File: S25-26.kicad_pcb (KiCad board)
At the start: 6 copper layers, 90 x 90 mm, 120 parts, among them IC1 CMV4000-3E5M0PN, IC10 DS90LV048ATM_NOPB, IC2 MXL86110I-AQB-R, IC3 NCV317BD2TR4G, IC4 MT29F2G01ABAGDWB-IT_G_TR, IC5 MT29F2G01ABAGDWB-IT_G_TR, IC6 XMC7200D-E272K8384AA, IC7 DS90LV011AHMF_NOPB, IC8 DS90LV048ATM_NOPB, IC9 DS90LV048ATM_NOPB, J1 DC_IN_PADS, J3 Conn_01x02_Pin, J4 RJ45_RB1-125B8G1A, Q1 ZXT849K, U1 TPS73601MDRBREP, U2 TPS73601MDRBREP, Y1 DSC1101DM2-012.0000

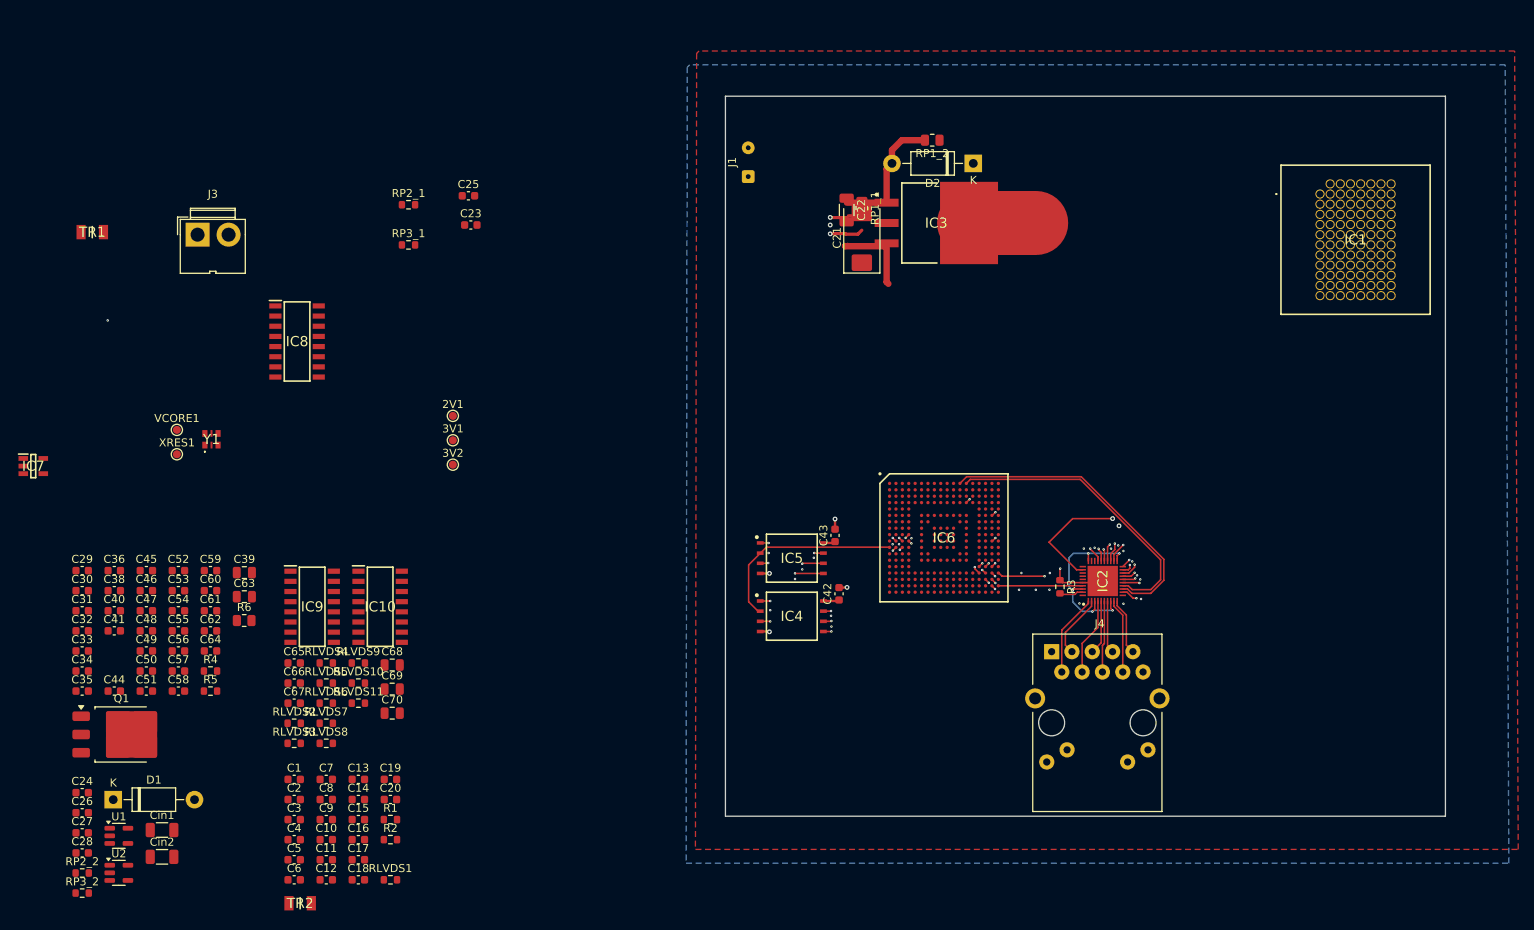
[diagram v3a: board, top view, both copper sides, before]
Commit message: Lots of PCB changes, some small parts changes
Updated parts footprints from those found in MDE Lab. Some parameters may be incorrect, but all footprints should be correct
Drew most of PCB. CMOS SPI still needs connection. Decoupling caps on MCU still need connection. Power and ground needs to be analyzed, and some components may not have power or ground connected.
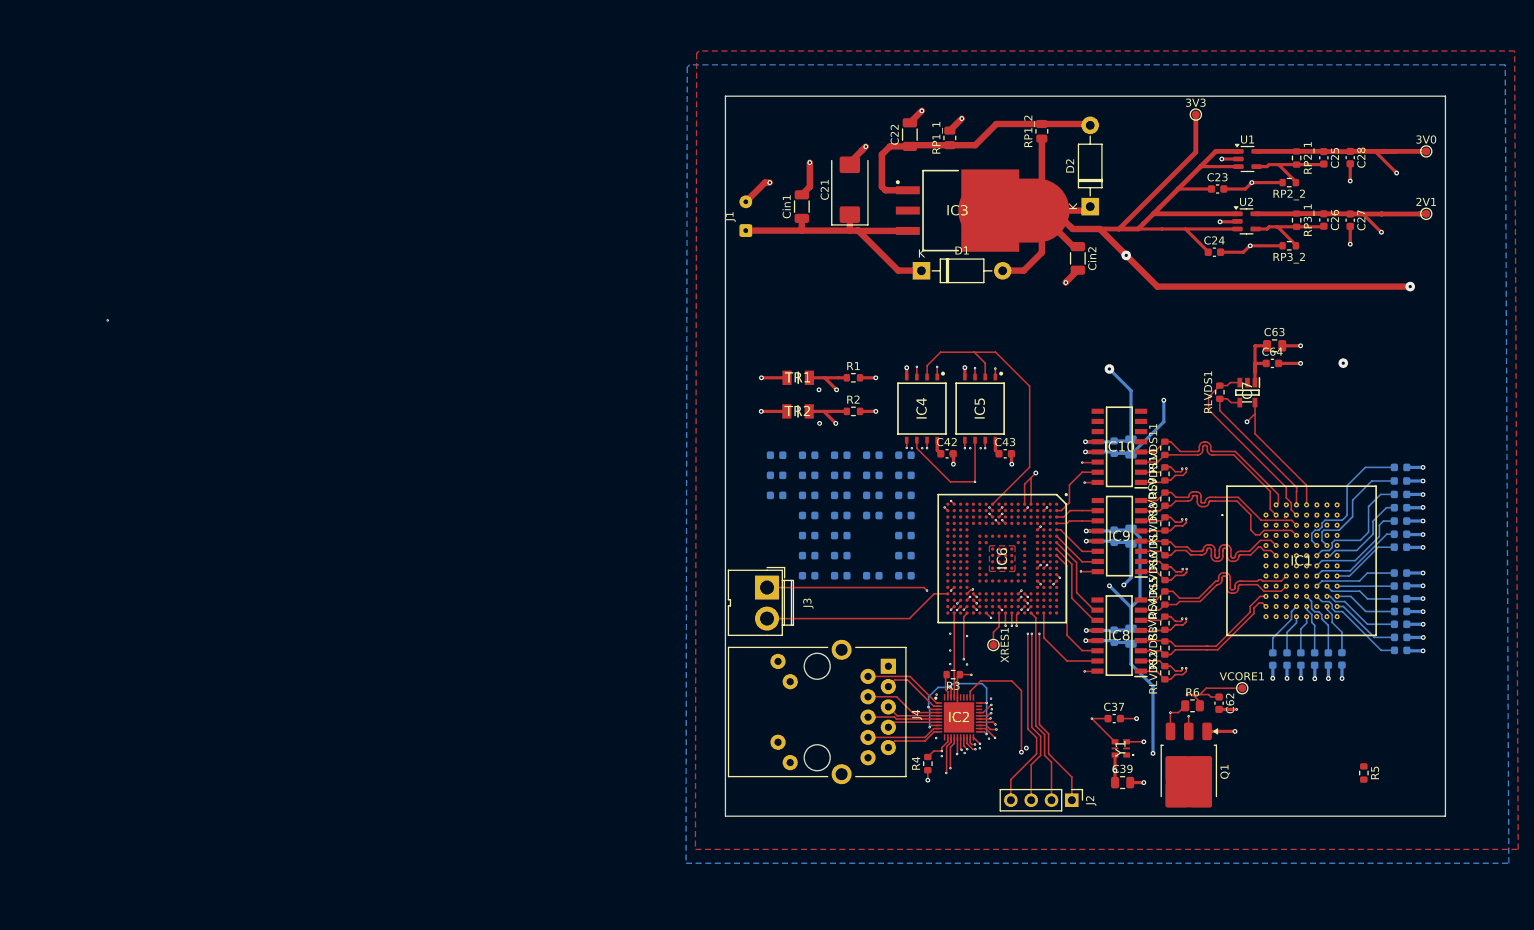
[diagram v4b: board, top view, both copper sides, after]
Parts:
- removed 3V1, 3V2: TestPoint, TestPoint:TestPoint_Pad_D1.0mm
- added 3V0: TestPoint, TestPoint:TestPoint_Pad_D1.0mm, F.Cu at (196.0, 57.1)
- added 3V3: TestPoint, TestPoint:TestPoint_Pad_D1.0mm, F.Cu at (167.2, 52.5)
- added C37: 15pF, Capacitor_SMD:C_0603_1608Metric, F.Cu at (157.0, 128.0)
- added J2: Conn_01x04_Pin, Connector_PinHeader_2.54mm:PinHeader_1x04_P2.54mm_Vertical, F.Cu at (151.7, 138.2)
- C1, C10, C11, C12, C13, C14, C15, C16, C17, C18, C19, C2, C20, C29, C3, C30, C31, C32, C33, C34, C35, C36, C38, C4, C40, C41, C44, C45, C46, C47, C48, C49, C5, C50, C51, C52, C53, C54, C55, C56, C57, C58, C59, C6, C60, C61, C65, C66, C67, C68, C69, C7, C70, C8, C9: moved to B.Cu
- moved C28 180.8 mm to (186.5, 57.9), turned to -90 degrees
- moved C27 176.0 mm to (186.5, 65.7), turned to -90 degrees
- moved RP2_2 173.8 mm to (178.9, 61.0), turned to 180 degrees
- moved C26 172.0 mm to (183.2, 65.7), turned to -90 degrees
- moved RP3_2 171.2 mm to (178.9, 68.9), turned to 180 degrees
- moved U1 164.5 mm to (173.7, 58.0)
- moved U2 162.8 mm to (173.5, 65.8)
- moved C24 156.8 mm to (169.5, 69.7)
- moved IC7 152.0 mm to (173.7, 87.2), turned to -90 degrees
- moved C5 146.7 mm to (192.8, 96.6), turned to 180 degrees
- moved C6 146.4 mm to (192.8, 100.0), turned to 180 degrees
- moved R5 144.5 mm to (188.2, 134.8), turned to -90 degrees
- moved C10 141.6 mm to (192.8, 98.3), turned to 180 degrees
- moved C11 141.3 mm to (192.8, 101.6), turned to 180 degrees
- moved C1 139.2 mm to (192.8, 119.5), turned to 180 degrees
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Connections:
- C47 pad 1: +3V3 -> /Processing/EXT_PS_CTL1
- C49 pad 1: +3V3 -> /Processing/EXT_PS_CTL1
- C51 pad 1: +3V3 -> /Processing/EXT_PS_CTL1
- C53 pad 1: +3V3 -> /Processing/EXT_PS_CTL1
- C54 pad 1: +3V3 -> /Processing/EXT_PS_CTL1
- C62 pad 1: +3V3 -> /Processing/EXT_PS_CTL1
- IC10 pad 1: /LVDS Conversion/LVDS_CLK_OUT_N -> /LVDS Conversion/LVDS_CH01_N
- IC10 pad 10: /LVDS Conversion/CMOS_CLK_OUT -> unconnected-(IC10-ROUT4-Pad10)
- IC10 pad 14: unconnected-(IC10-ROUT2-Pad14) -> /LVDS Conversion/CMOS_CTR_OUT
- IC10 pad 15: /LVDS Conversion/CMOS_CTR_OUT -> /LVDS Conversion/CMOS_CH01
- IC10 pad 2: /LVDS Conversion/LVDS_CLK_OUT_P -> /LVDS Conversion/LVDS_CH01_P
- IC10 pad 3: unconnected-(IC10-RIN2+-Pad3) -> /LVDS Conversion/LVDS_CTR_OUT_P
- IC10 pad 4: unconnected-(IC10-RIN2--Pad4) -> /LVDS Conversion/LVDS_CTR_OUT_N
- IC10 pad 7: /LVDS Conversion/LVDS_CTR_OUT_P -> unconnected-(IC10-RIN4+-Pad7)
- IC10 pad 8: /LVDS Conversion/LVDS_CTR_OUT_N -> unconnected-(IC10-RIN4--Pad8)
- IC6 pad A2: unconnected-(IC6B-P6.5-PadA2) -> /LVDS Conversion/CMOS_CH01
- IC6 pad A3: unconnected-(IC6B-P6.2-PadA3) -> /LVDS Conversion/CMOS_CH03
- IC6 pad A4: unconnected-(IC6B-P31.2-PadA4) -> /LVDS Conversion/CMOS_CH05
- IC6 pad A5: unconnected-(IC6B-P31.0-PadA5) -> /LVDS Conversion/CMOS_CH07
- IC6 pad A6: /LVDS Conversion/CMOS_CH01 -> /LVDS Conversion/CMOS_CH09
- IC6 pad A7: unconnected-(IC6B-P4.4-PadA7) -> /LVDS Conversion/CMOS_CH11
- IC6 pad A8: /LVDS Conversion/CMOS_CH03 -> /LVDS Conversion/CMOS_CH13
- IC6 pad A9: unconnected-(IC6B-P29.5-PadA9) -> /LVDS Conversion/CMOS_CH15
- IC6 pad B4: /Processing/TEMPR_ADC0 (P6.0) -> unconnected-(IC6B-P6.0-PadB4)
- IC6 pad B6: /LVDS Conversion/CMOS_CH11 -> unconnected-(IC6B-P5.1-PadB6)
- IC6 pad B8: /LVDS Conversion/CMOS_CH09 -> unconnected-(IC6B-P4.1-PadB8)
- IC6 pad C18: unconnected-(IC6B-P28.5-PadC18) -> /LVDS Conversion/CMOS_CLK_OUT
- IC6 pad C2: unconnected-(IC6B-P32.1-PadC2) -> /LVDS Conversion/CMOS_CTR_OUT
- IC6 pad C4: /Processing/TEMPR_ADC1 (P6.1) -> unconnected-(IC6B-P6.1-PadC4)
- IC6 pad C6: /LVDS Conversion/CMOS_CH05 -> unconnected-(IC6B-P5.2-PadC6)
- IC6 pad C8: /LVDS Conversion/CMOS_CH07 -> unconnected-(IC6B-P4.2-PadC8)
- IC6 pad D17: /LVDS Conversion/CMOS_CTR_OUT -> unconnected-(IC6B-P28.3-PadD17)
- IC6 pad D6: /LVDS Conversion/CMOS_CH15 -> unconnected-(IC6B-P5.3-PadD6)
- IC6 pad D8: /LVDS Conversion/CMOS_CH13 -> unconnected-(IC6B-P4.3-PadD8)
- IC6 pad F13: +3V3 -> /Processing/EXT_PS_CTL1
- IC6 pad F6: +3V3 -> /Processing/EXT_PS_CTL1
- IC6 pad G18: +3V3 -> /Processing/EXT_PS_CTL1
- IC6 pad J3: /LVDS Conversion/CMOS_CLK_OUT -> unconnected-(IC6B-P24.0-PadJ3)
- IC6 pad N13: +3V3 -> /Processing/EXT_PS_CTL1
- IC6 pad N6: +3V3 -> /Processing/EXT_PS_CTL1
- IC6 pad U1: unconnected-(IC6B-P12.6-PadU1) -> /Processing/TEMPR_ADC0 (P6.0)
- IC6 pad V2: unconnected-(IC6B-P13.0-PadV2) -> /Processing/TEMPR_ADC1 (P6.1)
- IC8 pad 1: /LVDS Conversion/LVDS_CH05_N -> /LVDS Conversion/LVDS_CLK_OUT_N
- IC8 pad 10: /LVDS Conversion/CMOS_CH13 -> /LVDS Conversion/CMOS_CH11
- IC8 pad 11: /LVDS Conversion/CMOS_CH07 -> /LVDS Conversion/CMOS_CH13
- IC8 pad 15: /LVDS Conversion/CMOS_CH05 -> /LVDS Conversion/CMOS_CLK_OUT
- IC8 pad 2: /LVDS Conversion/LVDS_CH05_P -> /LVDS Conversion/LVDS_CLK_OUT_P
- IC8 pad 5: /LVDS Conversion/LVDS_CH07_N -> /LVDS Conversion/LVDS_CH13_N
- IC8 pad 6: /LVDS Conversion/LVDS_CH07_P -> /LVDS Conversion/LVDS_CH13_P
- IC8 pad 7: /LVDS Conversion/LVDS_CH13_P -> /LVDS Conversion/LVDS_CH11_P
- IC8 pad 8: /LVDS Conversion/LVDS_CH13_N -> /LVDS Conversion/LVDS_CH11_N
- IC9 pad 1: /LVDS Conversion/LVDS_CH01_N -> /LVDS Conversion/LVDS_CH09_N
- IC9 pad 10: /LVDS Conversion/CMOS_CH09 -> /LVDS Conversion/CMOS_CH03
- IC9 pad 11: /LVDS Conversion/CMOS_CH03 -> /LVDS Conversion/CMOS_CH05
- IC9 pad 14: /LVDS Conversion/CMOS_CH11 -> /LVDS Conversion/CMOS_CH07
- IC9 pad 15: /LVDS Conversion/CMOS_CH01 -> /LVDS Conversion/CMOS_CH09
- IC9 pad 2: /LVDS Conversion/LVDS_CH01_P -> /LVDS Conversion/LVDS_CH09_P
- IC9 pad 3: /LVDS Conversion/LVDS_CH11_P -> /LVDS Conversion/LVDS_CH07_P
- IC9 pad 4: /LVDS Conversion/LVDS_CH11_N -> /LVDS Conversion/LVDS_CH07_N
- IC9 pad 5: /LVDS Conversion/LVDS_CH03_N -> /LVDS Conversion/LVDS_CH05_N
- IC9 pad 6: /LVDS Conversion/LVDS_CH03_P -> /LVDS Conversion/LVDS_CH05_P
- IC9 pad 7: /LVDS Conversion/LVDS_CH09_P -> /LVDS Conversion/LVDS_CH03_P
- IC9 pad 8: /LVDS Conversion/LVDS_CH09_N -> /LVDS Conversion/LVDS_CH03_N
- R6 pad 2: +3V3 -> /Processing/EXT_PS_CTL1
- RLVDS10 pad 1: /LVDS Conversion/LVDS_CLK_OUT_N -> /LVDS Conversion/LVDS_CH01_N
- RLVDS10 pad 2: /LVDS Conversion/LVDS_CLK_OUT_P -> /LVDS Conversion/LVDS_CH01_P
- RLVDS2 pad 1: /LVDS Conversion/LVDS_CH05_N -> /LVDS Conversion/LVDS_CLK_OUT_N
- RLVDS2 pad 2: /LVDS Conversion/LVDS_CH05_P -> /LVDS Conversion/LVDS_CLK_OUT_P
- RLVDS4 pad 1: /LVDS Conversion/LVDS_CH07_N -> /LVDS Conversion/LVDS_CH13_N
- RLVDS4 pad 2: /LVDS Conversion/LVDS_CH07_P -> /LVDS Conversion/LVDS_CH13_P
- RLVDS5 pad 1: /LVDS Conversion/LVDS_CH13_P -> /LVDS Conversion/LVDS_CH11_P
- RLVDS5 pad 2: /LVDS Conversion/LVDS_CH13_N -> /LVDS Conversion/LVDS_CH11_N
- RLVDS6 pad 1: /LVDS Conversion/LVDS_CH01_N -> /LVDS Conversion/LVDS_CH09_N
- RLVDS6 pad 2: /LVDS Conversion/LVDS_CH01_P -> /LVDS Conversion/LVDS_CH09_P
- RLVDS7 pad 1: /LVDS Conversion/LVDS_CH11_P -> /LVDS Conversion/LVDS_CH07_P
- RLVDS7 pad 2: /LVDS Conversion/LVDS_CH11_N -> /LVDS Conversion/LVDS_CH07_N
- RLVDS8 pad 1: /LVDS Conversion/LVDS_CH03_N -> /LVDS Conversion/LVDS_CH05_N
- RLVDS8 pad 2: /LVDS Conversion/LVDS_CH03_P -> /LVDS Conversion/LVDS_CH05_P
- RLVDS9 pad 1: /LVDS Conversion/LVDS_CH09_P -> /LVDS Conversion/LVDS_CH03_P
- RLVDS9 pad 2: /LVDS Conversion/LVDS_CH09_N -> /LVDS Conversion/LVDS_CH03_N
- VCORE1 pad 1: +3V3 -> /Processing/EXT_PS_CTL1
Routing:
- net GND: track 19.9 -> 462.0 mm, vias 35 -> 67
- net +3V3: track 11.9 -> 451.2 mm, vias 0 -> 17
- net +3V: track 0.00 -> 94.7 mm, vias 0 -> 1
- net +2V1: track 0.00 -> 80.8 mm, vias 0 -> 1
- net /CMOS_MASTER_CLK: track 0.00 -> 53.7 mm, vias 0 -> 2
- net /Processing/EXT_PS_CTL1: track 0.00 -> 38.2 mm, vias 0 -> 2
- net /LVDS Conversion/LVDS_RECV_EN: track 0.00 -> 36.5 mm, vias 0 -> 4
- net Net-(D2-A): track 0.00 -> 35.1 mm
- net /Processing/DRV_VOUT: track 0.00 -> 31.2 mm, vias 0 -> 2
- net /Processing/EXT_PS_CTL0: track 0.00 -> 30.8 mm, vias 0 -> 2
- net /Processing/TEMPR_ADC0 (P6.0): track 0.00 -> 30.0 mm, vias 0 -> 2
- net /JTAG_SWCLK: track 0.00 -> 28.2 mm, vias 0 -> 2
- net /Processing/TEMPR_ADC1 (P6.1): track 0.00 -> 26.7 mm, vias 0 -> 2
- net /JTAG_SWO: track 0.00 -> 26.3 mm, vias 0 -> 2
- net /JTAG_TDI: track 0.00 -> 26.2 mm, vias 0 -> 2
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- added copper zone on F.Cu, net GND

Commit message: Adjusted board setup for AdvancedPCB; fixed many DRC errors
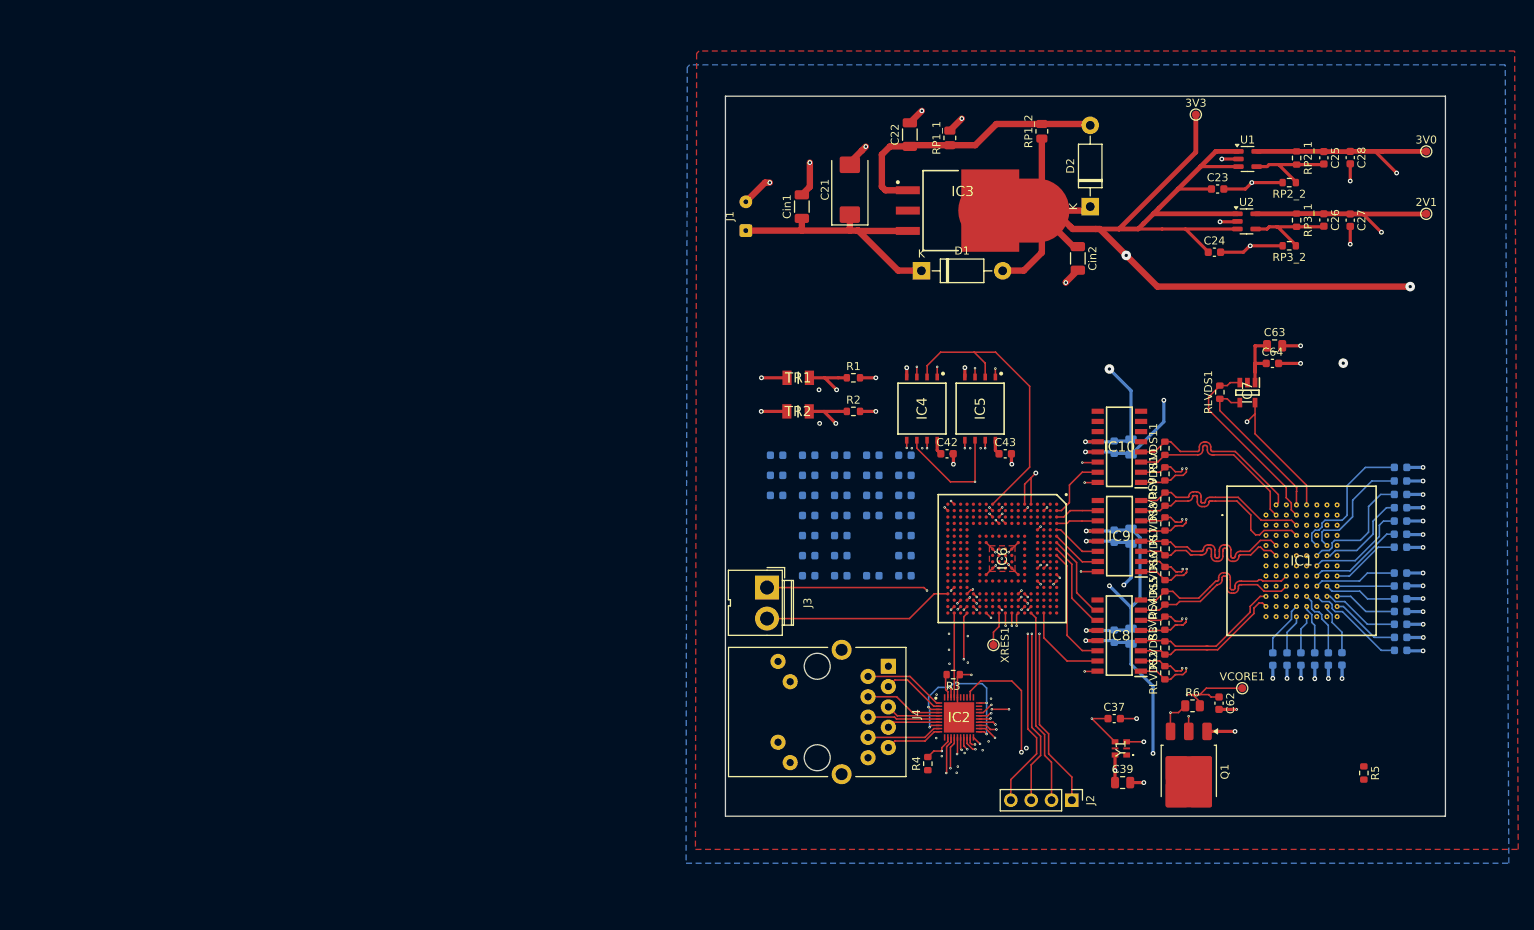
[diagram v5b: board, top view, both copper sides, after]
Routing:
- net GND: track 462.0 -> 473.6 mm, vias 67 -> 75
- net /ETH0_TXD_2: track 27.1 -> 28.9 mm
- net +3V: track 94.7 -> 93.1 mm
- net +3V3: track 451.2 -> 450.0 mm, vias 17 -> 16
- net /ETH0_TXD_0: track 21.3 -> 22.3 mm
- net (no net): vias 1 -> 0

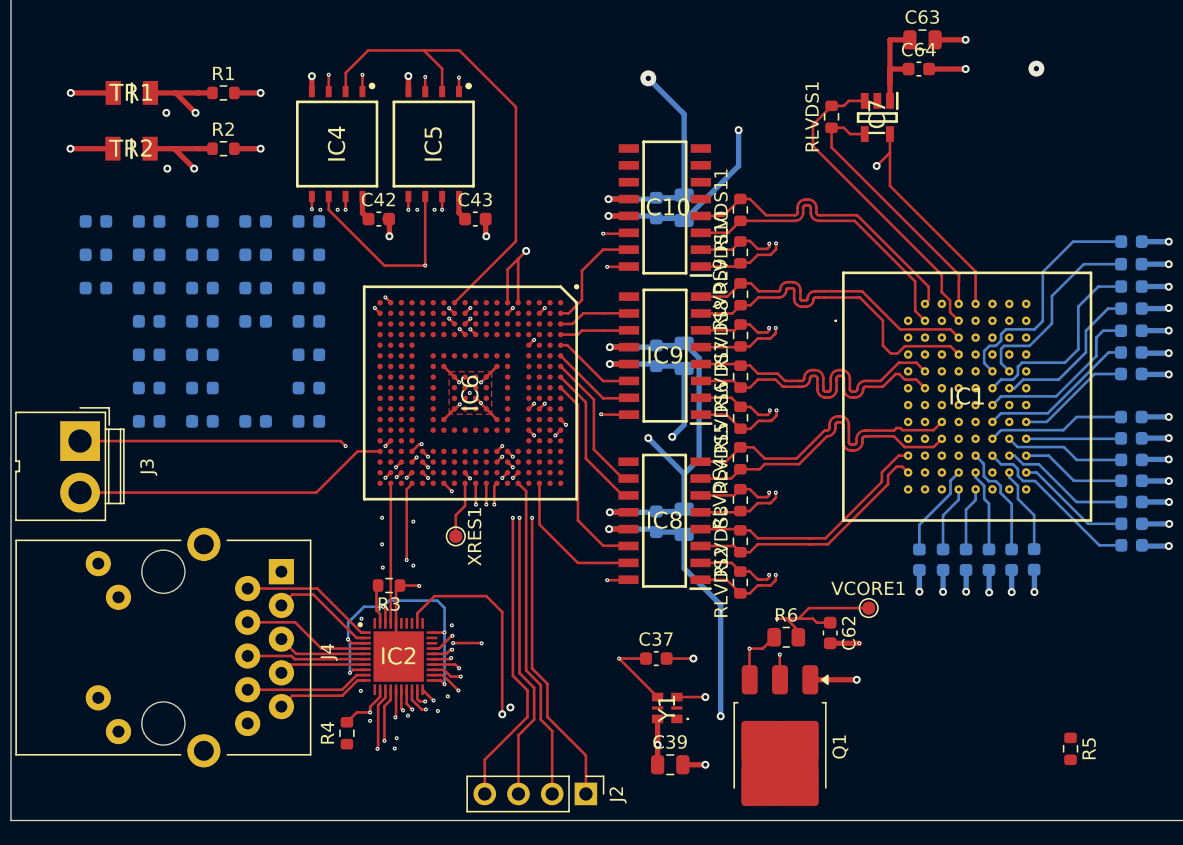
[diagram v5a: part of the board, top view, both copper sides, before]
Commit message: Fixed DRC; all connections made
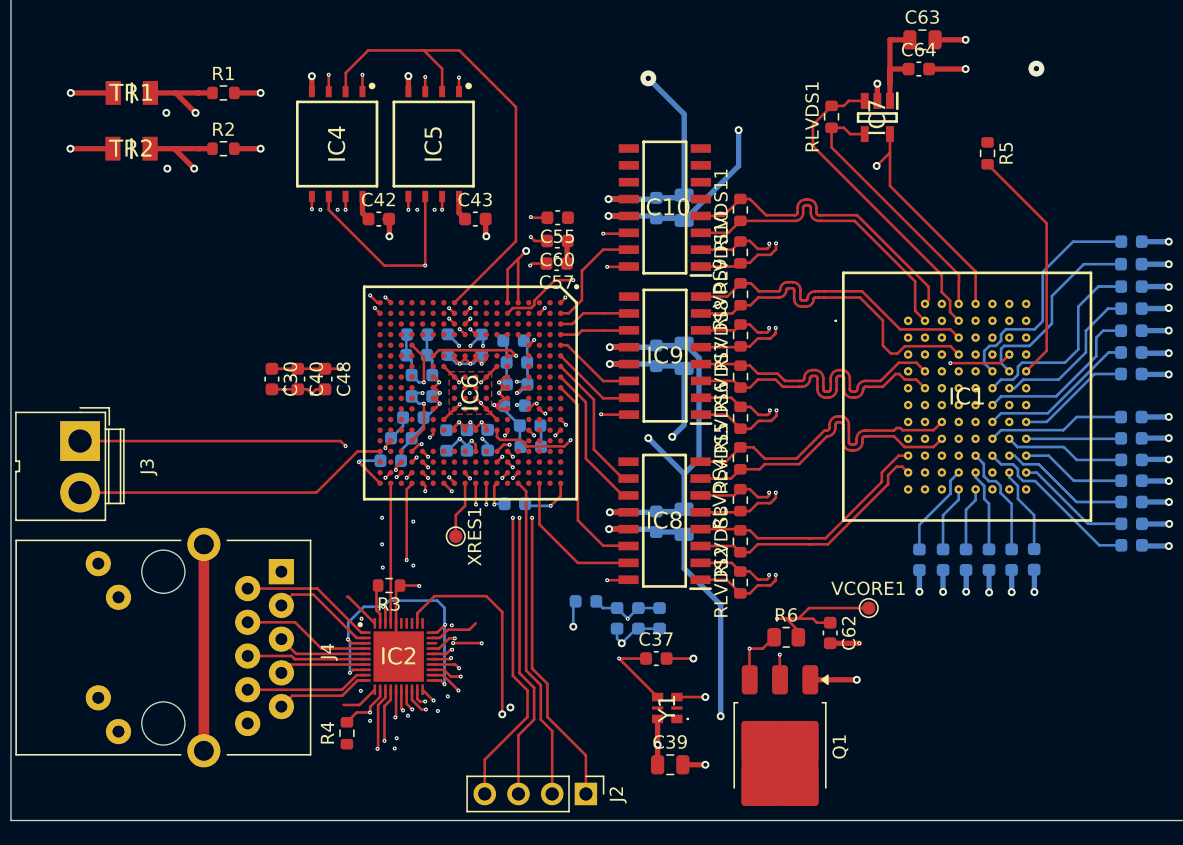
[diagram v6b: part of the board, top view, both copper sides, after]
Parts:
- C30, C40, C48, C55, C57, C60: moved to F.Cu
- moved R5 45.3 mm to (181.9, 90.0)
- moved C53 44.6 mm to (154.1, 125.0), turned to -90 degrees
- moved C54 44.5 mm to (155.7, 125.0), turned to -90 degrees
- moved C47 42.5 mm to (157.2, 125.0), turned to -90 degrees
- moved C60 34.8 mm to (149.6, 96.5)
- moved C61 34.3 mm to (147.5, 110.5), turned to 0 degrees
- moved C57 32.1 mm to (149.5, 98.2)
- moved C51 31.9 mm to (151.7, 123.7)
- moved C55 31.7 mm to (149.6, 94.8)
- moved C52 28.9 mm to (146.2, 104.0), turned to 0 degrees
- moved C58 28.8 mm to (147.6, 112.0), turned to 0 degrees
- moved C59 28.6 mm to (137.0, 113.1)
- moved C49 26.1 mm to (146.3, 116.3), turned to 0 degrees
- moved C50 23.8 mm to (146.5, 105.7), turned to 0 degrees
- moved C45 21.7 mm to (138.7, 109.8)
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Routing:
- net +3V3: track 450.0 -> 535.9 mm, vias 16 -> 29
- net GND: track 473.6 -> 553.8 mm, vias 75 -> 101
- net /CMOS_SPI_MOSI: track 0.57 -> 67.4 mm
- net /CMOS_SPI_MISO: track 0.57 -> 64.2 mm
- net /CMOS_RESET_N: track 0.57 -> 59.6 mm
- net /CMOS_SPI_CLK: track 0.00 -> 58.2 mm, vias 0 -> 1
- net /FRAME_REQ: track 0.57 -> 43.7 mm
- net /CMOS_SPI_EN: track 0.57 -> 41.8 mm, vias 1 -> 2
- net /Processing/EXT_PS_CTL1: track 38.2 -> 70.7 mm, vias 2 -> 6
- net unconnected-(J4-PadSH): track 0.00 -> 15.5 mm
- added copper zone on In4.Cu, net +3V3
